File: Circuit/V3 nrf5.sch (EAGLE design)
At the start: 59 parts, among them J4 USB Micro, J7 CORTEX_DEBUG_SMD, Q1 BSS138, U1 AL8805, U2 MCP73831, U3 BC840M, U4 3.3V/150mA, U5 AL8805, U6 AL8805, U7 MP3414AGJ-Z

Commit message: Adding Digikey part numbers to all 40 components. Total BOM: .04. Also switching 5V boost controller IC due to availability.
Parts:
- removed C9: 1uF, SparkFun:CAP0603-CAP
- removed LED1: Red, SparkFun:LED0603
- removed R11: 1K, SparkFun:RESISTOR0603-RES
- removed R15: 4.7k, SparkFun-Resistors:4.7KOHM-0603-1/10W-1%
- removed U7: MP3414AGJ-Z, MP3414AGJ-Z:MP3414AGJ-Z
- added C1: 10uF, SparkFun-Capacitors:22UF-0805-6.3V-20%
- added C3: 22uF, SparkFun-Capacitors:22UF-0805-6.3V-20%
- added C6: 1uF, SparkFun-Capacitors:22UF-0805-6.3V-20%
- added R14: 1k, SparkFun-Resistors:1KOHM-0603-1/10W-1%
- added U8: TPS61235PRWLR, TPS61235PRWLR:TPS61235PRWLR
- C10, C12: DIGIKEY (none) -> 399-3482-1-ND
- C11: DIGIKEY (none) -> 718-1131-1-ND
- C13: value 22uF 16V X7R -> 22uF
- C14, C4, C8: DIGIKEY (none) -> 399-6374-1-ND
- C15: value 1uF 16V X7R -> 22uF
- C16: value 22uF -> 1uF; DIGIKEY 1276-6471-2-ND -> GRM188R60J106ME84D
- C2, C5, C7: DIGIKEY (none) -> 399-1254-1-ND
- D1: DIGIKEY (none) -> 160-1184-1-ND
- D2: DIGIKEY (none) -> 160-1837-1-ND
- D3: DIGIKEY (none) -> 160-1183-1-ND
- D4, D5, D6, D7, D8: DIGIKEY (none) -> B340A-E3/61TGICT-ND
- D9: DIGIKEY (none) -> 160-1436-1-ND
- J1, J2, J3: DIGIKEY (none) -> 277-1721-ND
- J4: device 2040002-1:2040002-1 -> 1050170001:1050170001; DIGIKEY (none) -> 1050170001
- J6: DIGIKEY (none) -> 277-1860-ND
- J7: DIGIKEY (none) -> SAM1161-05-ND
- L1, L2, L3: DIGIKEY (none) -> SRN6045TA-330MCT-ND
- L4: value 1.5uH 5A -> 1.0 uH; device SparkFun-Passives:INDUCTORBOURNS_SRN6045 -> FDSD0630-H-1R0M_P3:FDSD0630-H-1R0M=P3; DIGIKEY 587-2097-2-ND -> 490-10878-1-ND
- POWER_IN: DIGIKEY (none) -> A100080CT-ND
- Q1: DIGIKEY (none) -> BSS138CT-ND
- R1, R3, R9: DIGIKEY (none) -> A138521CT-ND
- R10: DIGIKEY (none) -> A130088CT-ND
- R12, R2, R8: DIGIKEY (none) -> P10KGCT-ND
- R13: value 110k -> 332k; DIGIKEY (none) -> RMCF0603FT332K
- R4, R6: DIGIKEY (none) -> P330HCT-ND
- R5: DIGIKEY (none) -> P1.0KGCT-ND
- R7: value 909K -> 1M; DIGIKEY (none) -> RMCF0603FT1M00
- RPROG: DIGIKEY (none) -> P2.00KHCT-ND
- S1: DIGIKEY (none) -> CKN12222-1-ND
- S3: DIGIKEY (none) -> 563-1102-1-ND
- U1, U5, U6: DIGIKEY (none) -> AL8805W5-7DICT-ND
- U2: DIGIKEY (none) -> MCP73831T-2ACI/OTCT-ND
- U3: DIGIKEY (none) -> 1914-BC840MCT-ND
- U4: DIGIKEY (none) -> 576-1259-1-ND
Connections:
- removed net N$38: LED1.A, R11.1
- new net N$6: U8.CC
- net 3V3: now also C6.1; no longer C9.1
- net 5V: now also C3.1, U8.VOUT; no longer R11.2, U7.OUT
- net 5VIN: now also J4.1; no longer J4.VBUS
- net GND: now also C1.2, C3.2, C6.2, J4.5, R14.2, U8.AGND, U8.INACT, U8.PGND; no longer C9.2, J4.GND, LED1.C, R15.1, U7.AGND, U7.PGND
- net N$13: now also R14.1; no longer R15.2
- net N$3: now also U8.SW; no longer U7.SW
- net N$9: now also U8.FB; no longer U7.FB
- net VBATT_ON: now also C1.1, U8.EN, U8.VIN; no longer U7.EN, U7.IN
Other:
- moved on the sheet: C15, C16, J4, S3

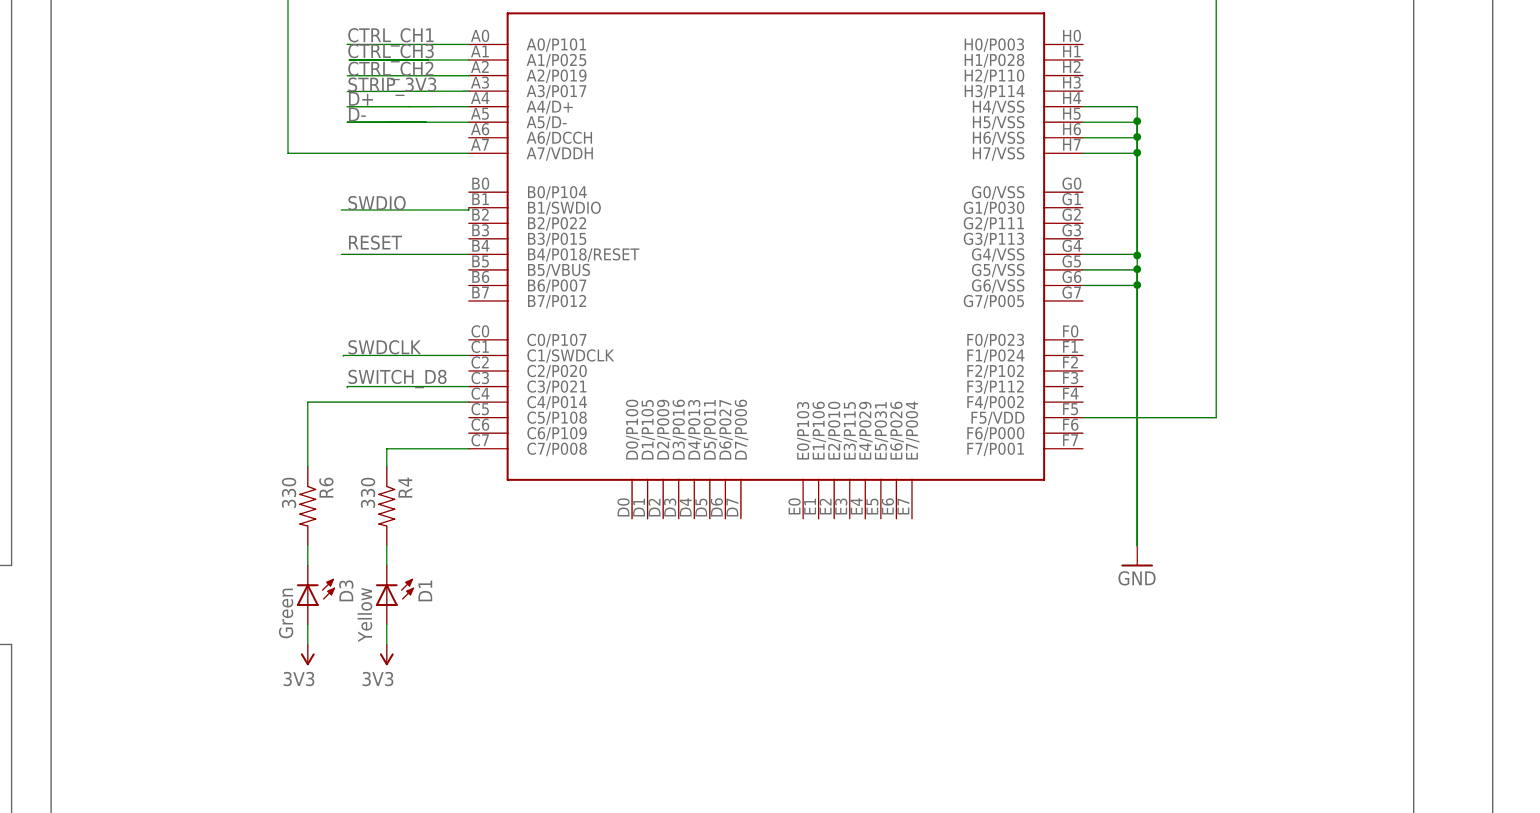
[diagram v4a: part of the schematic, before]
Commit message: Adding a 32.768k crystal (and 22pF bypass caps for a 12.5pF capacitive load). Need to move the battery around and make room for the button.
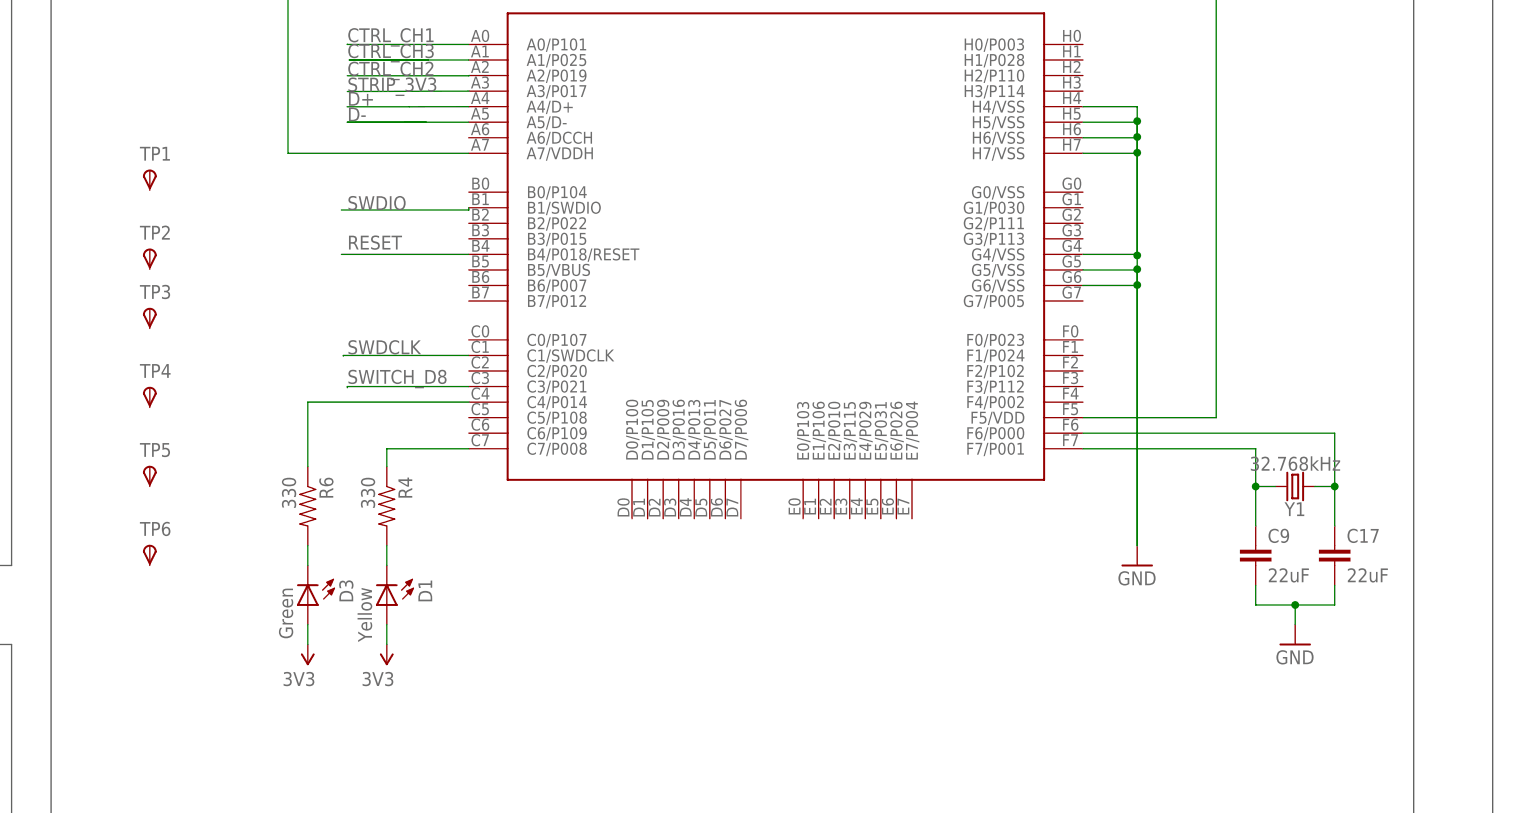
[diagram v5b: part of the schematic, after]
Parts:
- added C17, C9: 22uF, SparkFun-Capacitors:22UF-0805-6.3V-20%
- added TP1, TP2, TP3, TP4, TP5, TP6: TPSB1,27, testpad:TPSB1,27
- added Y1: 32.768kHz, SparkFun-Clocks:CRYSTAL-32.768KHZSMD-3.2X1.5
- R14, R5: DIGIKEY P1.0KGCT-ND -> RMCF0603FG1K00
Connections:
- new net N$10: C9.1, U3.F7/P001, Y1.2
- new net N$8: C17.1, U3.F6/P000, Y1.1
- net GND: now also C17.2, C9.2
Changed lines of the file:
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@@
 </part>
 <part name="R5" library="SparkFun-Resistors" deviceset="1KOHM" device="-0603-1/10W-1%" value="1k">
-<attribute name="DIGIKEY" value="P1.0KGCT-ND"/>
+<attribute name="DIGIKEY" value="RMCF0603FG1K00"/>
 </part>
 <part name="GND3" library="SparkFun-PowerSymbols" deviceset="GND" device=""/>
@@
 <part name="GND27" library="SparkFun" deviceset="GND" device=""/>
 <part name="R14" library="SparkFun-Resistors" deviceset="1KOHM" device="-0603-1/10W-1%" value="1k">
-<attribute name="DIGIKEY" value="P1.0KGCT-ND"/>
+<attribute name="DIGIKEY" value="RMCF0603FG1K00"/>
 </part>
 <part name="C6" library="SparkFun-Capacitors" deviceset="22UF" device="-0805-6.3V-20%" value="1uF">
 <attribute name="DIGIKEY" value="GRM188R60J106ME84D"/>
+</part>
+<part name="TP1" library="testpad" library_urn="urn:adsk.eagle:library:385" deviceset="TPS" device="B1,27" package3d_urn="urn:adsk.eagle:package:27944/2"/>
+<part name="TP2" library="testpad" library_urn="urn:adsk.eagle:library:385" deviceset="TPS" device="B1,27" package3d_urn="urn:adsk.eagle:package:27944/2"/>
+<part name="TP3" library="testpad" library_urn="urn:adsk.eagle:library:385" deviceset="TPS" device="B1,27" package3d_urn="urn:adsk.eagle:package:27944/2"/>
+<part name="TP4" library="testpad" library_urn="urn:adsk.eagle:library:385" deviceset="TPS" device="B1,27" package3d_urn="urn:adsk.eagle:package:27944/2"/>
+<part name="TP5" library="testpad" library_urn="urn:adsk.eagle:library:385" deviceset="TPS" device="B1,27" package3d_urn="urn:adsk.eagle:package:27944/2"/>
+<part name="TP6" library="testpad" library_urn="urn:adsk.eagle:library:385" deviceset="TPS" device="B1,27" package3d_urn="urn:adsk.eagle:package:27944/2"/>
+<part name="Y1" library="SparkFun-Clocks" library_urn="urn:adsk.eagle:library:511" deviceset="CRYSTAL-32.768KHZ" device="SMD-3.2X1.5" package3d_urn="urn:adsk.eagle:package:37548/1" value="32.768kHz">
+<attribute name="DIGIKEY" value="1923-1342-1-ND"/>
+</part>
+<part name="GND28" library="SparkFun" deviceset="GND" device=""/>
+<part name="C9" library="SparkFun-Capacitors" deviceset="22UF" device="-0805-6.3V-20%" value="22uF">
+<attribute name="DIGIKEY" value="1276-6780-2-ND"/>
+</part>
+<part name="C17" library="SparkFun-Capacitors" deviceset="22UF" device="-0805-6.3V-20%" value="22uF">
+<attribute name="DIGIKEY" value="1276-6780-2-ND"/>
 </part>
 </parts>
@@
 <attribute name="DIGIKEY" x="401.32" y="25.4" size="1.778" layer="96" display="off"/>
 </instance>
+<instance part="TP1" gate="G$1" x="12.7" y="147.32" smashed="yes">
+<attribute name="NAME" x="11.43" y="148.59" size="1.778" layer="95"/>
+<attribute name="TP_SIGNAL_NAME" x="13.97" y="146.05" size="1.778" layer="97"/>
+</instance>
+<instance part="TP2" gate="G$1" x="12.7" y="137.16" smashed="yes">
+<attribute name="NAME" x="11.43" y="138.43" size="1.778" layer="95"/>
+<attribute name="TP_SIGNAL_NAME" x="13.97" y="135.89" size="1.778" layer="97"/>
+</instance>
+<instance part="TP3" gate="G$1" x="12.7" y="129.54" smashed="yes">
+<attribute name="NAME" x="11.43" y="130.81" size="1.778" layer="95"/>
+<attribute name="TP_SIGNAL_NAME" x="13.97" y="128.27" size="1.778" layer="97"/>
+</instance>
+<instance part="TP4" gate="G$1" x="12.7" y="119.38" smashed="yes">
+<attribute name="NAME" x="11.43" y="120.65" size="1.778" layer="95"/>
+<attribute name="TP_SIGNAL_NAME" x="13.97" y="118.11" size="1.778" layer="97"/>
+</instance>
+<instance part="TP5" gate="G$1" x="12.7" y="109.22" smashed="yes">
+<attribute name="NAME" x="11.43" y="110.49" size="1.778" layer="95"/>
+<attribute name="TP_SIGNAL_NAME" x="13.97" y="107.95" size="1.778" layer="97"/>
+</instance>
+<instance part="TP6" gate="G$1" x="12.7" y="99.06" smashed="yes">
+<attribute name="NAME" x="11.43" y="100.33" size="1.778" layer="95"/>
+<attribute name="TP_SIGNAL_NAME" x="13.97" y="97.79" size="1.778" layer="97"/>
+</instance>
+<instance part="Y1" gate="G$1" x="160.02" y="106.68" smashed="yes" rot="R180">
+<attribute name="NAME" x="160.02" y="104.648" size="1.778" layer="95" font="vector" rot="R180" align="bottom-center"/>
+<attribute name="VALUE" x="160.02" y="108.712" size="1.778" layer="96" font="vector" rot="R180" align="top-center"/>
+<attribute name="DIGIKEY" x="160.02" y="106.68" size="3.4798" layer="96" ratio="10" rot="R180" display="off"/>
+</instance>
+<instance part="GND28" gate="1" x="160.02" y="86.36" smashed="yes">
+<attribute name="VALUE" x="157.48" y="83.82" size="1.778" layer="96"/>
+</instance>
+<instance part="C9" gate="G$1" x="154.94" y="96.52" smashed="yes">
+<attribute name="NAME" x="156.464" y="99.441" size="1.778" layer="95" font="vector"/>
+<attribute name="VALUE" x="156.464" y="94.361" size="1.778" layer="96" font="vector"/>
+<attribute name="DIGIKEY" x="154.94" y="96.52" size="1.778" layer="96" display="off"/>
+</instance>
+<instance part="C17" gate="G$1" x="165.1" y="96.52" smashed="yes">
+<attribute name="NAME" x="166.624" y="99.441" size="1.778" layer="95" font="vector"/>
+<attribute name="VALUE" x="166.624" y="94.361" size="1.778" layer="96" font="vector"/>
+<attribute name="DIGIKEY" x="165.1" y="96.52" size="1.778" layer="96" display="off"/>
+</instance>
 </instances>
 <busses>
@@
 <pinref part="GND27" gate="1" pin="GND"/>
 </segment>
+<segment>
+<pinref part="C9" gate="G$1" pin="2"/>
+<wire x1="154.94" y1="93.98" x2="154.94" y2="91.44" width="0.1524" layer="91"/>
+<wire x1="154.94" y1="91.44" x2="160.02" y2="91.44" width="0.1524" layer="91"/>
+<pinref part="GND28" gate="1" pin="GND"/>
+<wire x1="160.02" y1="91.44" x2="160.02" y2="88.9" width="0.1524" layer="91"/>
+<pinref part="C17" gate="G$1" pin="2"/>
+<wire x1="165.1" y1="93.98" x2="165.1" y2="91.44" width="0.1524" layer="91"/>
+<wire x1="165.1" y1="91.44" x2="160.02" y2="91.44" width="0.1524" layer="91"/>
+<junction x="160.02" y="91.44"/>
+</segment>
 </net>
 <net name="RESET" class="0">
@@
 </segment>
 </net>
+<net name="N$8" class="0">
+<segment>
+<pinref part="U3" gate="G$1" pin="F6/P000"/>
+<pinref part="C17" gate="G$1" pin="1"/>
+<wire x1="132.726" y1="113.534" x2="165.1" y2="113.534" width="0.1524" layer="91"/>
+<wire x1="165.1" y1="113.534" x2="165.1" y2="106.68" width="0.1524" layer="91"/>
+<pinref part="Y1" gate="G$1" pin="1"/>
+<wire x1="165.1" y1="106.68" x2="165.1" y2="101.6" width="0.1524" layer="91"/>
+<wire x1="162.56" y1="106.68" x2="165.1" y2="106.68" width="0.1524" layer="91"/>
+<junction x="165.1" y="106.68"/>
+</segment>
+</net>
+<net name="N$10" class="0">
+<segment>
+<pinref part="U3" gate="G$1" pin="F7/P001"/>
+<pinref part="C9" gate="G$1" pin="1"/>
+<wire x1="132.726" y1="111.534" x2="154.94" y2="111.534" width="0.1524" layer="91"/>
+<wire x1="154.94" y1="111.534" x2="154.94" y2="106.68" width="0.1524" layer="91"/>
+<pinref part="Y1" gate="G$1" pin="2"/>
+<wire x1="154.94" y1="106.68" x2="154.94" y2="101.6" width="0.1524" layer="91"/>
+<wire x1="154.94" y1="106.68" x2="157.48" y2="106.68" width="0.1524" layer="91"/>
+<junction x="154.94" y="106.68"/>
+</segment>
+</net>

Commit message: Submitting fourth board iteration. Moved components around to work better in enclosure. New USB connector, new 5V booster, added four test points, and moved pins around to match BSP on board (buttons and leds).
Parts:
- removed TP5, TP6: TPSB1,27, testpad:TPSB1,27
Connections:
- removed net 3.3V: U3.A7/VDDH
- removed net SWITCH_D8: R8.2, S1.2, U3.C3/P021
- new net SWITCH_1: R8.2, S1.2, U3.D5/P011
- net 3V3: now also R8.1, TP1.PP, U3.A7/VDDH; no longer S1.1
- net 5V: now also TP2.PP
- net CTRL_CH1: now also U3.C4/P014; no longer U3.A0/P101
- net CTRL_CH2: now also U3.B3/P015; no longer U3.A2/P019
- net CTRL_CH3: now also U3.D3/P016; no longer U3.A1/P025
- net GND: now also S1.1; no longer R8.1
- net N$4: now also U3.D4/P013; no longer U3.C4/P014
- net STRIP_3V3: now also TP4.PP
- net VBATT: now also TP3.PP
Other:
- moved on the sheet: C10, D1, D2, D3, R4, R5, R6, R8, TP1, TP2, TP3, TP4

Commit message: Updating Gerbers.
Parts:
- J4: DIGIKEY 1050170001 -> WM1399CT-ND
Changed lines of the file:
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@@
 </part>
 <part name="J4" library="1050170001" deviceset="1050170001" device="" value="USB Micro">
-<attribute name="DIGIKEY" value="1050170001"/>
+<attribute name="DIGIKEY" value="WM1399CT-ND"/>
 </part>
 <part name="S3" library="SparkFun-Switches" library_urn="urn:adsk.eagle:library:535" deviceset="SWITCH-SPDT" device="-SMD-RIGHT-ANGLE" package3d_urn="urn:adsk.eagle:package:40179/1">

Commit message: Updating digikey part numbers to better match board.
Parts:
- C1: DIGIKEY GRM188R60J106ME84D -> 399-4925-1-ND
- C13, C15, C17, C3, C9: DIGIKEY 1276-6780-2-ND -> 490-10511-1-ND
- C6: DIGIKEY GRM188R60J106ME84D -> 399-8006-1-ND
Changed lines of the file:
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@@
 </part>
 <part name="C13" library="SparkFun-Capacitors" deviceset="22UF" device="-0805-6.3V-20%" value="22uF">
-<attribute name="DIGIKEY" value="1276-6780-2-ND"/>
+<attribute name="DIGIKEY" value="490-10511-1-ND"/>
 </part>
 <part name="C15" library="SparkFun-Capacitors" deviceset="22UF" device="-0805-6.3V-20%" value="22uF">
-<attribute name="DIGIKEY" value="1276-6780-2-ND"/>
+<attribute name="DIGIKEY" value="490-10511-1-ND"/>
 </part>
 <part name="C16" library="SparkFun-Capacitors" deviceset="22UF" device="-0805-6.3V-20%" value="1uF">
@@
 <part name="GND21" library="SparkFun" deviceset="GND" device=""/>
 <part name="C1" library="SparkFun-Capacitors" deviceset="22UF" device="-0805-6.3V-20%" value="10uF">
-<attribute name="DIGIKEY" value="GRM188R60J106ME84D"/>
+<attribute name="DIGIKEY" value="399-4925-1-ND"/>
 </part>
 <part name="GND24" library="SparkFun" deviceset="GND" device=""/>
 <part name="C3" library="SparkFun-Capacitors" deviceset="22UF" device="-0805-6.3V-20%" value="22uF">
-<attribute name="DIGIKEY" value="1276-6780-2-ND"/>
+<attribute name="DIGIKEY" value="490-10511-1-ND"/>
 </part>
 <part name="GND27" library="SparkFun" deviceset="GND" device=""/>
@@
 </part>
 <part name="C6" library="SparkFun-Capacitors" deviceset="22UF" device="-0805-6.3V-20%" value="1uF">
-<attribute name="DIGIKEY" value="GRM188R60J106ME84D"/>
+<attribute name="DIGIKEY" value="399-8006-1-ND"/>
 </part>
 <part name="TP1" library="testpad" library_urn="urn:adsk.eagle:library:385" deviceset="TPS" device="B1,27" package3d_urn="urn:adsk.eagle:package:27944/2"/>
@@
 <part name="GND28" library="SparkFun" deviceset="GND" device=""/>
 <part name="C9" library="SparkFun-Capacitors" deviceset="22UF" device="-0805-6.3V-20%" value="22uF">
-<attribute name="DIGIKEY" value="1276-6780-2-ND"/>
+<attribute name="DIGIKEY" value="490-10511-1-ND"/>
 </part>
 <part name="C17" library="SparkFun-Capacitors" deviceset="22UF" device="-0805-6.3V-20%" value="22uF">
-<attribute name="DIGIKEY" value="1276-6780-2-ND"/>
+<attribute name="DIGIKEY" value="490-10511-1-ND"/>
 </part>
 <part name="P+1" library="SparkFun" deviceset="3.3V" device="" value="3V3"/>
@@
 </sheet>
 </sheets>
-<errors>
-</errors>
 </schematic>
 </drawing>
